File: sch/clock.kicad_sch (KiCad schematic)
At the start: 8 parts, among them U2 74AHC74, U3 SN74LVC1G14DBV

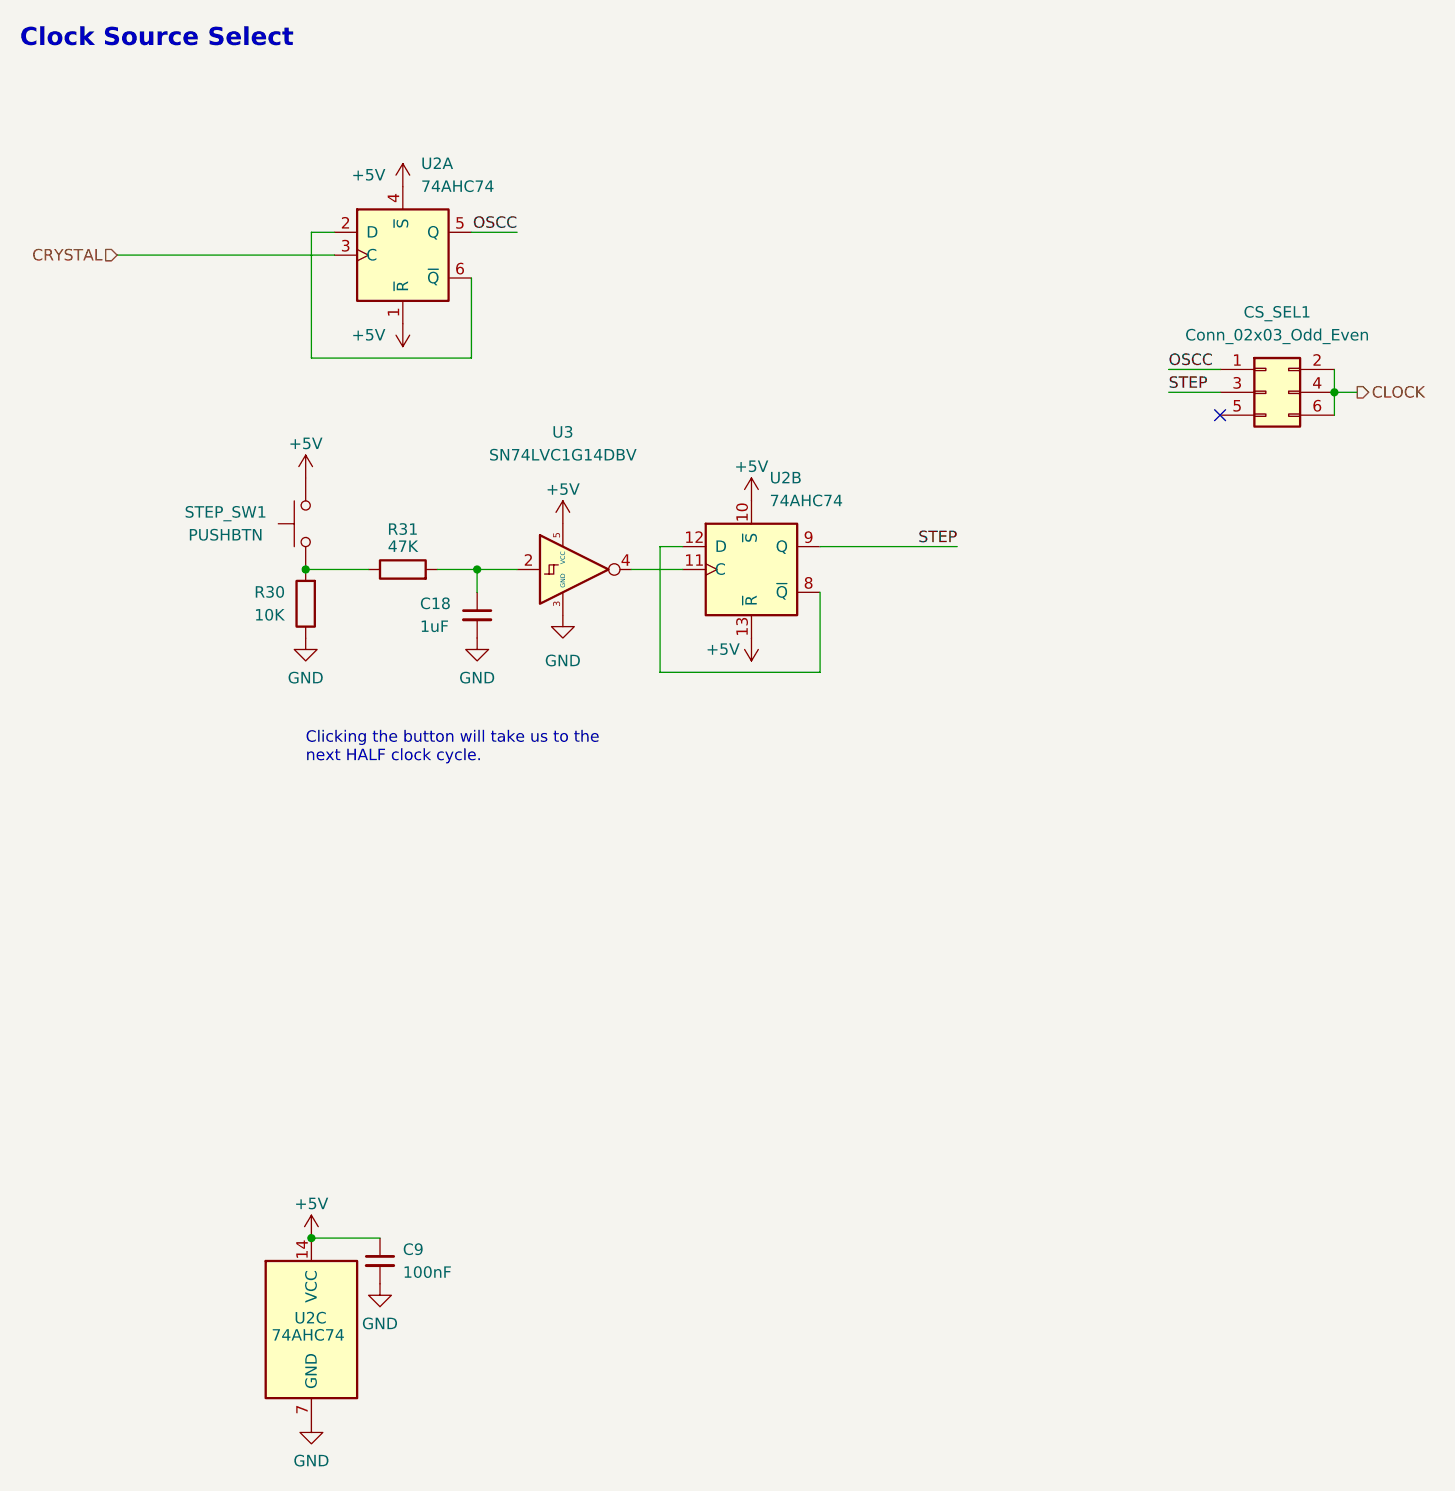
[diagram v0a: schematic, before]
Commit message: update schematic
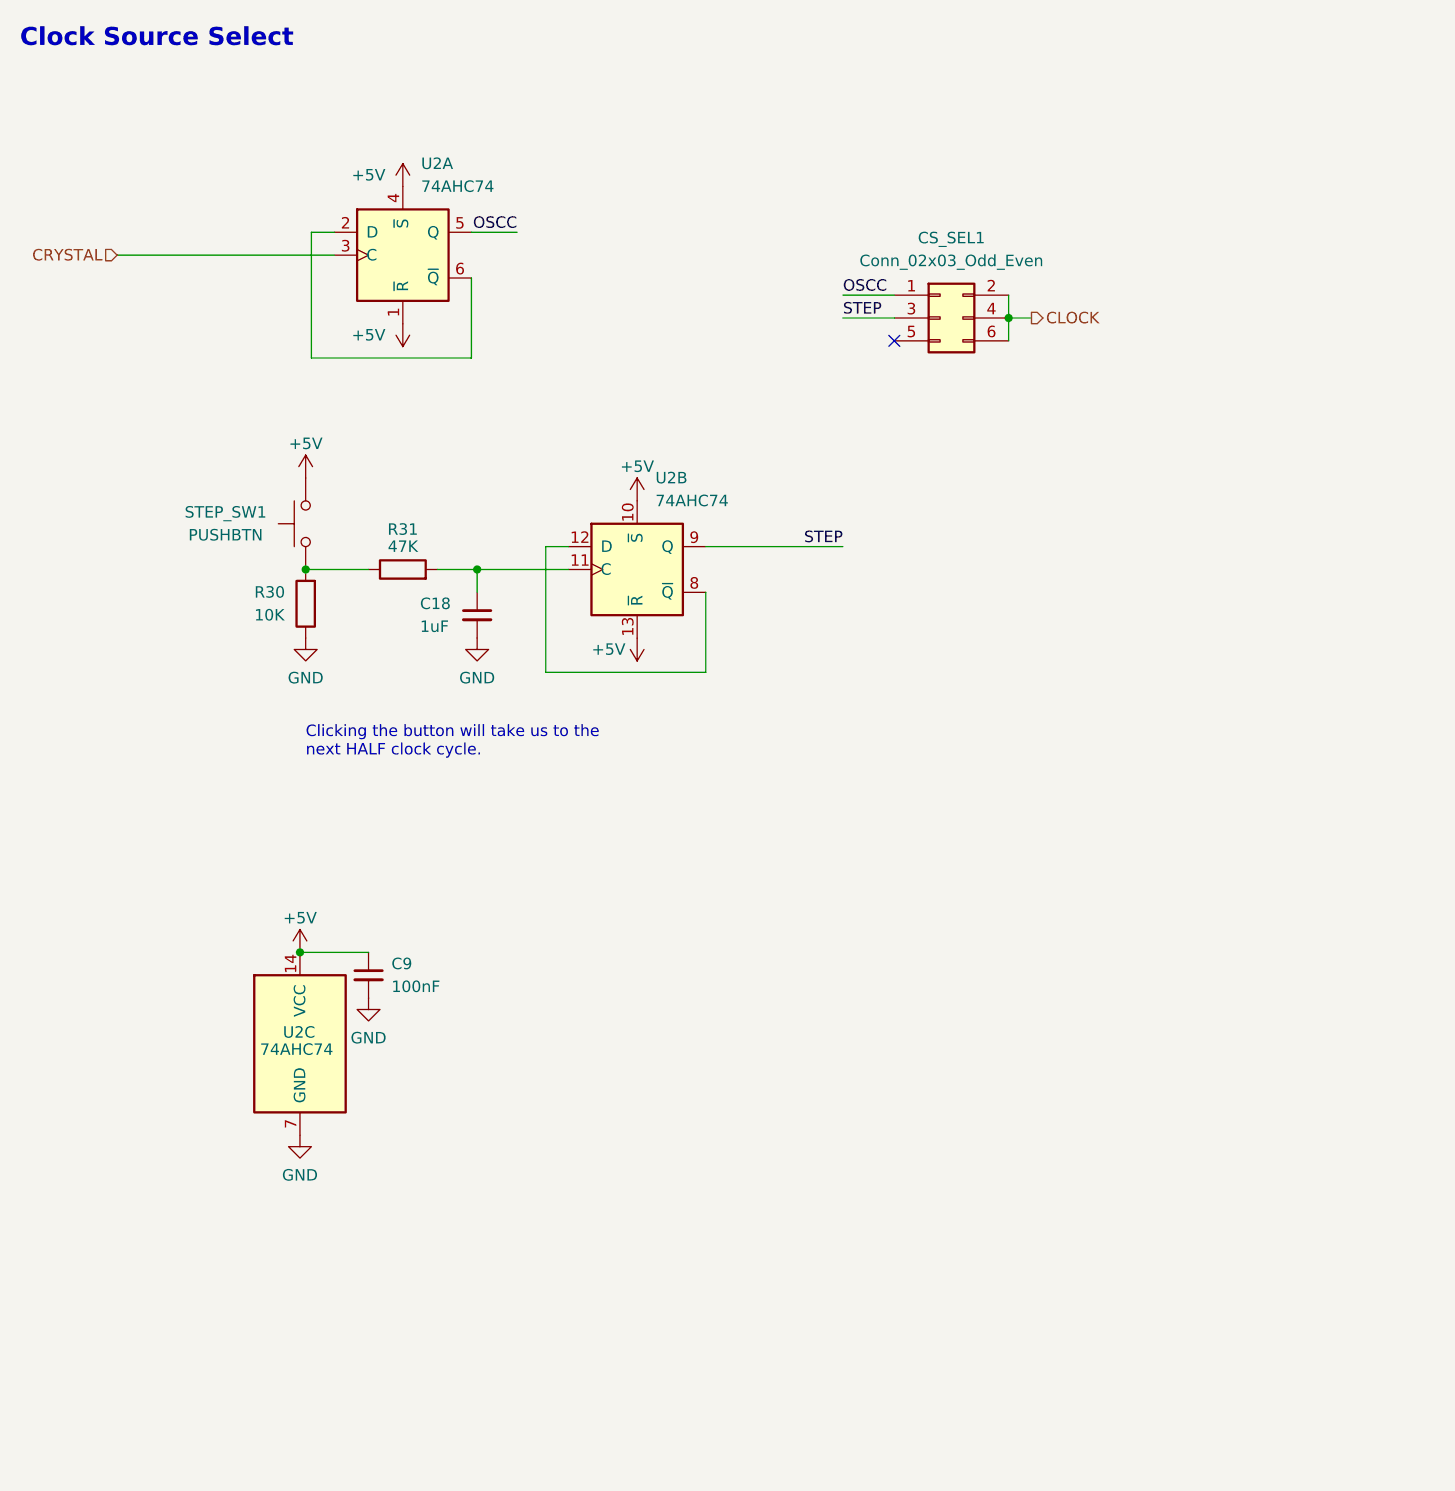
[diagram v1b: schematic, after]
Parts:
- removed U3: SN74LVC1G14DBV, Package_TO_SOT_SMD:SOT-23-5, symbol 74xGxx:SN74LVC1G14DBV
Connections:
- net at U2.11 (C): now also C18.1, R31.2
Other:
- moved on the sheet: C9, CS_SEL1, U2B, U2C

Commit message: Cleanup board
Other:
- moved on the sheet: R31
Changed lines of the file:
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@@
     (stroke (width 0) (type default) (color 0 0 0 0))
   )
-  (wire (pts (xy 63.5 83.185) (xy 70.485 83.185))
+  (wire (pts (xy 63.5 83.185) (xy 69.215 83.185))
     (stroke (width 0) (type default) (color 0 0 0 0))
   )
@@
     (stroke (width 0) (type default) (color 0 0 0 0))
   )
-  (wire (pts (xy 78.105 83.185) (xy 82.55 83.185))
+  (wire (pts (xy 76.835 83.185) (xy 82.55 83.185))
     (stroke (width 0) (type default) (color 0 0 0 0))
   )
@@
     (pin "2")
   )
-  (symbol (lib_id "Device:R") (at 74.295 83.185 90) (unit 1)
+  (symbol (lib_id "Device:R") (at 73.025 83.185 90) (unit 1)
     (in_bom yes) (on_board yes)
-    (property "Reference" "R31" (id 0) (at 74.295 78.74 90))
-    (property "Value" "47K" (id 1) (at 74.295 80.645 90))
-    (property "Footprint" "Resistor_SMD:R_0805_2012Metric" (id 2) (at 74.295 84.963 90)
-      (effects (font (size 1.27 1.27)) hide)
-    )
-    (property "Datasheet" "~" (id 3) (at 74.295 83.185 0)
-      (effects (font (size 1.27 1.27)) hide)
-    )
+    (property "Reference" "R31" (id 0) (at 73.025 78.74 90))
+    (property "Value" "47K" (id 1) (at 73.025 80.645 90))
+    (property "Footprint" "Resistor_SMD:R_0805_2012Metric" (id 2) (at 73.025 84.963 90)
+      (effects (font (size 1.27 1.27)) hide)
+    )
+    (property "Datasheet" "~" (id 3) (at 73.025 83.185 0)
+      (effects (font (size 1.27 1.27)) hide)
+    )

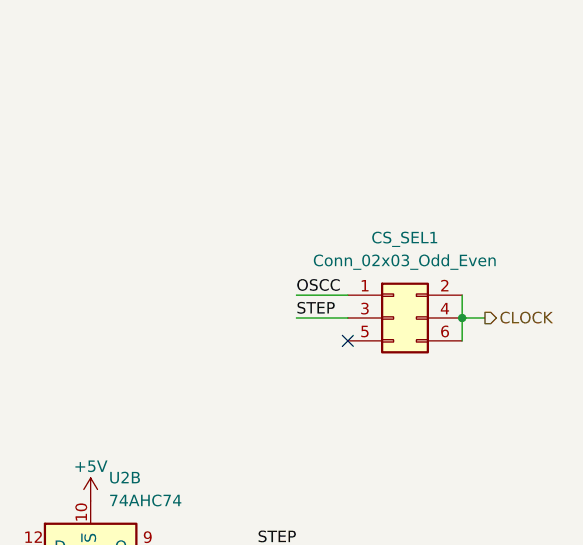
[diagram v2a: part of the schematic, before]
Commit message: bigger header pins
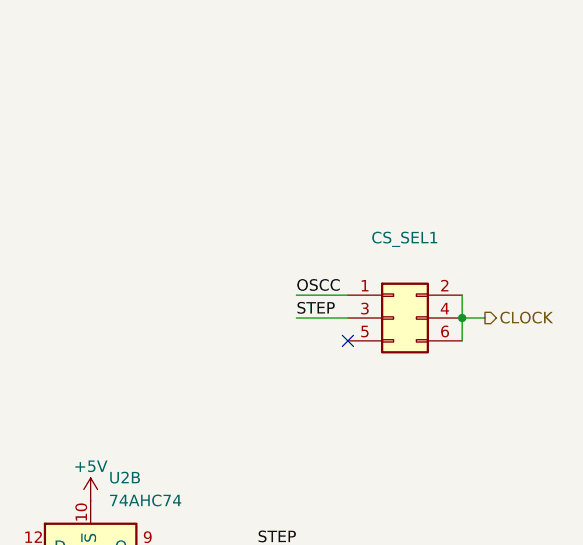
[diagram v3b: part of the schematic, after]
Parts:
- CS_SEL1: value Conn_02x03_Odd_Even -> (none); footprint Connector_PinHeader_2.00mm:PinHeader_2x03_P2.00mm_Vertical -> (none)
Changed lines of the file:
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@@
     (in_bom yes) (on_board yes) (fields_autoplaced)
     (property "Reference" "CS_SEL1" (id 0) (at 135.255 46.355 0))
-    (property "Value" "Conn_02x03_Odd_Even" (id 1) (at 135.255 48.895 0))
-    (property "Footprint" "Connector_PinHeader_2.00mm:PinHeader_2x03_P2.00mm_Vertical" (id 2) (at 133.985 55.245 0)
+    (property "Value" "" (id 1) (at 135.255 48.895 0))
+    (property "Footprint" "" (id 2) (at 133.985 55.245 0)
       (effects (font (size 1.27 1.27)) hide)
     )

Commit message: small updates
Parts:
- CS_SEL1: value (none) -> Conn_02x03_Odd_Even; footprint (none) -> Connector_PinHeader_2.54mm:PinHeader_2x03_P2.54mm_Vertical
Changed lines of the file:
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@@
   )
   (text "Clock Source Select" (at 31.75 25.4 0)
-    (effects (font (size 2 2) bold) (justify left bottom))
+    (effects (font (size 2 2) (thickness 0.254) bold) (justify left bottom))
   )
   (label "STEP" (at 123.19 55.245 0)
@@
     (in_bom yes) (on_board yes) (fields_autoplaced)
     (property "Reference" "CS_SEL1" (id 0) (at 135.255 46.355 0))
-    (property "Value" "" (id 1) (at 135.255 48.895 0))
-    (property "Footprint" "" (id 2) (at 133.985 55.245 0)
+    (property "Value" "Conn_02x03_Odd_Even" (id 1) (at 135.255 48.895 0))
+    (property "Footprint" "Connector_PinHeader_2.54mm:PinHeader_2x03_P2.54mm_Vertical" (id 2) (at 133.985 55.245 0)
       (effects (font (size 1.27 1.27)) hide)
     )
